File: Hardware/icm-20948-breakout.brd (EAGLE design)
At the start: 19.3 x 10.5 mm, 11 parts, among them J1 455-1750-1-ND, J2 455-1750-1-ND, U1 NCP563, U2 NTS0104, U3 ICM-20948

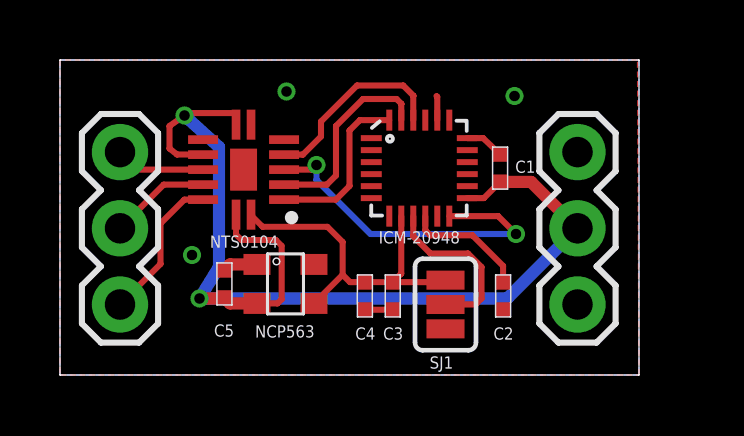
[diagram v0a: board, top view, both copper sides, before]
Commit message: Remake to fit 0.7 inch width.
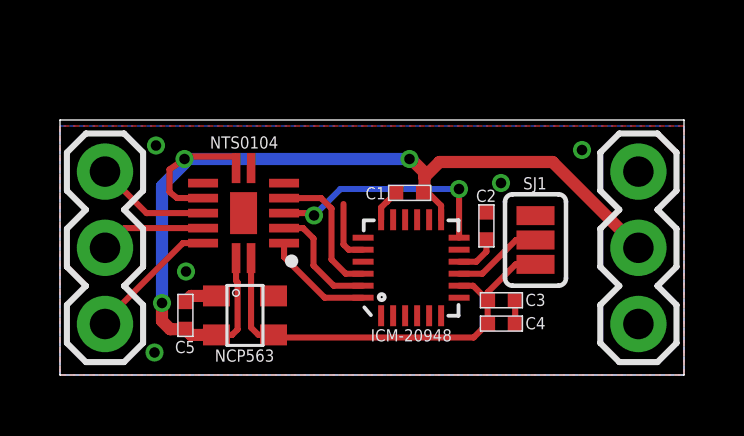
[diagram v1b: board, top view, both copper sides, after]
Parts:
- moved C4 4.64 mm to (14.7, 1.71), turned to 0 degrees
- moved SJ1 3.69 mm to (15.8, 4.50), turned to 90 degrees
- moved C3 3.62 mm to (14.7, 2.49), turned to 0 degrees
- moved U3 3.33 mm to (11.7, 3.58), turned to 90 degrees
- moved C1 3.13 mm to (11.7, 6.07), turned to 180 degrees
- moved C2 2.40 mm to (14.2, 4.97), turned to 90 degrees
- moved J2 2.13 mm to (19.3, 1.70)
- moved U1 1.71 mm to (6.17, 1.99)
- moved C5 1.67 mm to (4.18, 1.99)
- moved U2 1.45 mm to (6.12, 5.40)
- moved J1 0.82 mm to (1.50, 1.70)
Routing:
- net INT3-1_8: track 11.5 -> 7.86 mm
- net VDD1_8: track 11.8 -> 14.7 mm
- net SCL3-1_8: track 6.67 -> 3.96 mm
- net N$2: track 5.70 -> 3.01 mm
- net N$1: track 4.10 -> 1.45 mm
- net VCC: track 36.6 -> 34.2 mm, vias 2 -> 3
- net SDA3-1_8: track 5.69 -> 3.66 mm
- net CS-1_8: track 6.51 -> 4.67 mm
- net GND: track 4.35 -> 5.20 mm, vias 3 -> 5
- net INT3: track 3.01 -> 3.84 mm
- net SDA3: track 5.01 -> 4.44 mm
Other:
- board size 19.3 x 10.5 mm -> 20.8 x 8.5 mm

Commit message: Changed DRC settings to get vias covered.
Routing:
- net GND: track 5.20 -> 5.86 mm
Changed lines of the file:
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@@
 </class>
 </classes>
-<designrules name="oshpark-2layer">
+<designrules name="oshpark-2layer *">
 <description language="en">&lt;b&gt;OSH Park Design Rules&lt;/b&gt;
 &lt;p&gt;
@@
 <param name="mlMinCreamFrame" value="0mil"/>
 <param name="mlMaxCreamFrame" value="0mil"/>
-<param name="mlViaStopLimit" value="0mil"/>
+<param name="mlViaStopLimit" value="14mil"/>
 <param name="srRoundness" value="0"/>
 <param name="srMinRoundness" value="0mil"/>
@@
 <contactref element="U3" pad="20"/>
 <wire x1="15.174" y1="1.714" x2="15.174" y2="2.492" width="0.2032" layer="1"/>
-<wire x1="10.8987875" y1="5.78" x2="10.904" y2="5.78" width="0.2032" layer="1"/>
-<wire x1="10.904" y1="5.78" x2="11.194" y2="6.07" width="0.2032" layer="1"/>
-<wire x1="10.704" y1="5.176" x2="10.704" y2="5.5852125" width="0.2032" layer="1"/>
-<wire x1="10.704" y1="5.5852125" x2="10.8987875" y2="5.78" width="0.2032" layer="1"/>
 <wire x1="5.216" y1="2.636" x2="4.37" y2="2.636" width="0.4064" layer="1"/>
 <wire x1="4.37" y1="2.636" x2="4.18" y2="2.446" width="0.4064" layer="1"/>
@@
 <via x="3.2" y="7.65" extent="1-16" drill="0.35"/>
 <via x="17.4" y="7.5" extent="1-16" drill="0.35"/>
-<wire x1="10.104" y1="4.176" x2="9.624" y2="4.176" width="0.2032" layer="1"/>
-<wire x1="9.624" y1="4.176" x2="9.45" y2="4.35" width="0.2032" layer="1"/>
-<wire x1="9.45" y1="4.35" x2="9.45" y2="5.7" width="0.2032" layer="1"/>
 <via x="3.15" y="0.75" extent="1-16" drill="0.35"/>
-<wire x1="10.704" y1="5.176" x2="10.104" y2="4.176" width="0" layer="19" extent="1-1"/>
+<wire x1="10.8987875" y1="5.78" x2="10.904" y2="5.78" width="0.2032" layer="1"/>
+<wire x1="10.904" y1="5.78" x2="11.194" y2="6.07" width="0.2032" layer="1"/>
+<wire x1="10.704" y1="5.176" x2="10.704" y2="5.5852125" width="0.2032" layer="1"/>
+<wire x1="10.704" y1="5.5852125" x2="10.8987875" y2="5.78" width="0.2032" layer="1"/>
+<wire x1="10.104" y1="4.176" x2="9.524" y2="4.176" width="0.2032" layer="1"/>
+<wire x1="9.45" y1="4.25" x2="9.45" y2="6.3" width="0.2032" layer="1"/>
+<wire x1="9.524" y1="4.176" x2="9.45" y2="4.25" width="0.2032" layer="1"/>
 </signal>
 <signal name="VCC">
@@
 <mfgpreviewcolor name="substratecolor" color="0xFF786E46"/>
 </mfgpreviewcolors>
-<errors>
-</errors>
 </board>
 </drawing>

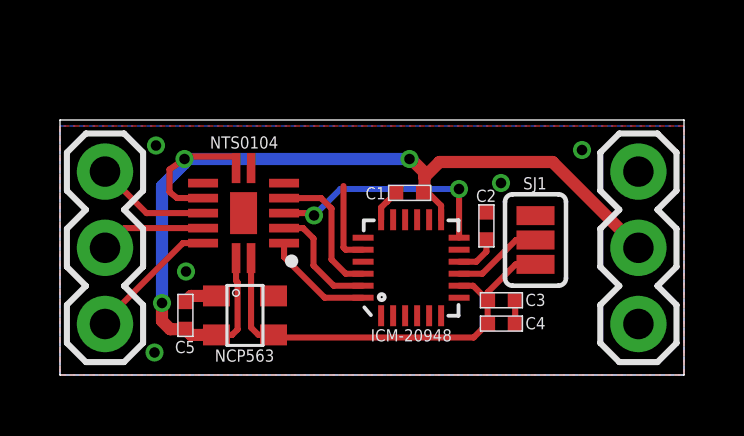
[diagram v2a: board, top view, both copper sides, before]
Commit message: Went back to 0.6 inch width. Took away ground plane under icm. Added AD0 as an output pin with pull-up and therefore removed solder jumper.
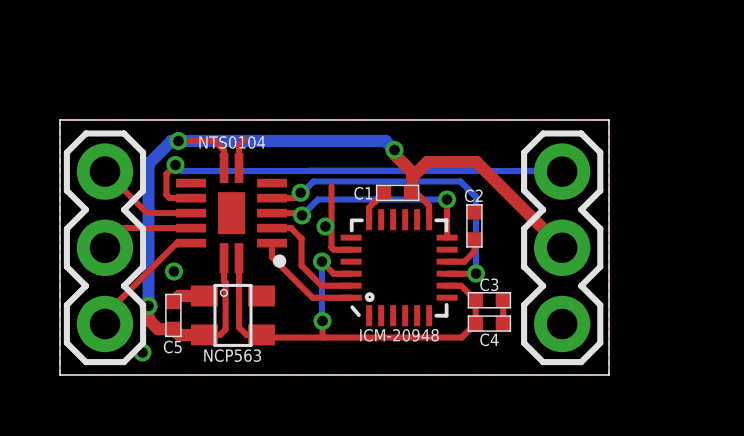
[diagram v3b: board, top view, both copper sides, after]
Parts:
- removed SJ1: JUMPER-32-3, SparkFun-Passives:SJ_3_PASTE2&3
- moved J2 2.54 mm to (16.7, 1.70)
- moved C1 0.40 mm to (11.3, 6.07)
- moved C2 0.40 mm to (13.8, 4.97)
- moved C3 0.40 mm to (14.3, 2.49)
- moved C4 0.40 mm to (14.3, 1.71)
- moved U1 0.40 mm to (5.77, 1.99)
- moved U3 0.40 mm to (11.3, 3.58)
- moved C5 0.40 mm to (3.78, 1.99)
- moved U2 0.40 mm to (5.72, 5.40)
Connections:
- removed net CS-1_8: U2.5, U3.22
- removed net N$2: SJ1.2, U3.9
- new net AD0: J2.3, U2.10
- new net AD0-1_8: U2.5, U3.9
- net GND: no longer SJ1.3
- net VCC: no longer U2.10
- net VDD1_8: now also U3.22; no longer SJ1.1
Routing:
- net AD0: track 0.00 -> 15.0 mm, vias 0 -> 1
- net AD0-1_8: track 0.00 -> 10.8 mm, vias 0 -> 2
- net CS-1_8: track 4.67 -> 0.00 mm
- net VCC: track 34.2 -> 31.0 mm
- net N$2: track 3.01 -> 0.00 mm
- net VDD1_8: track 14.7 -> 16.2 mm, vias 0 -> 2
- net GND: track 5.86 -> 6.89 mm, vias 5 -> 3
- net INT3-1_8: track 7.86 -> 7.36 mm
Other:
- board size 20.8 x 8.5 mm -> 18.3 x 8.5 mm
